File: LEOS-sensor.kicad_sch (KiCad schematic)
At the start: 3 parts

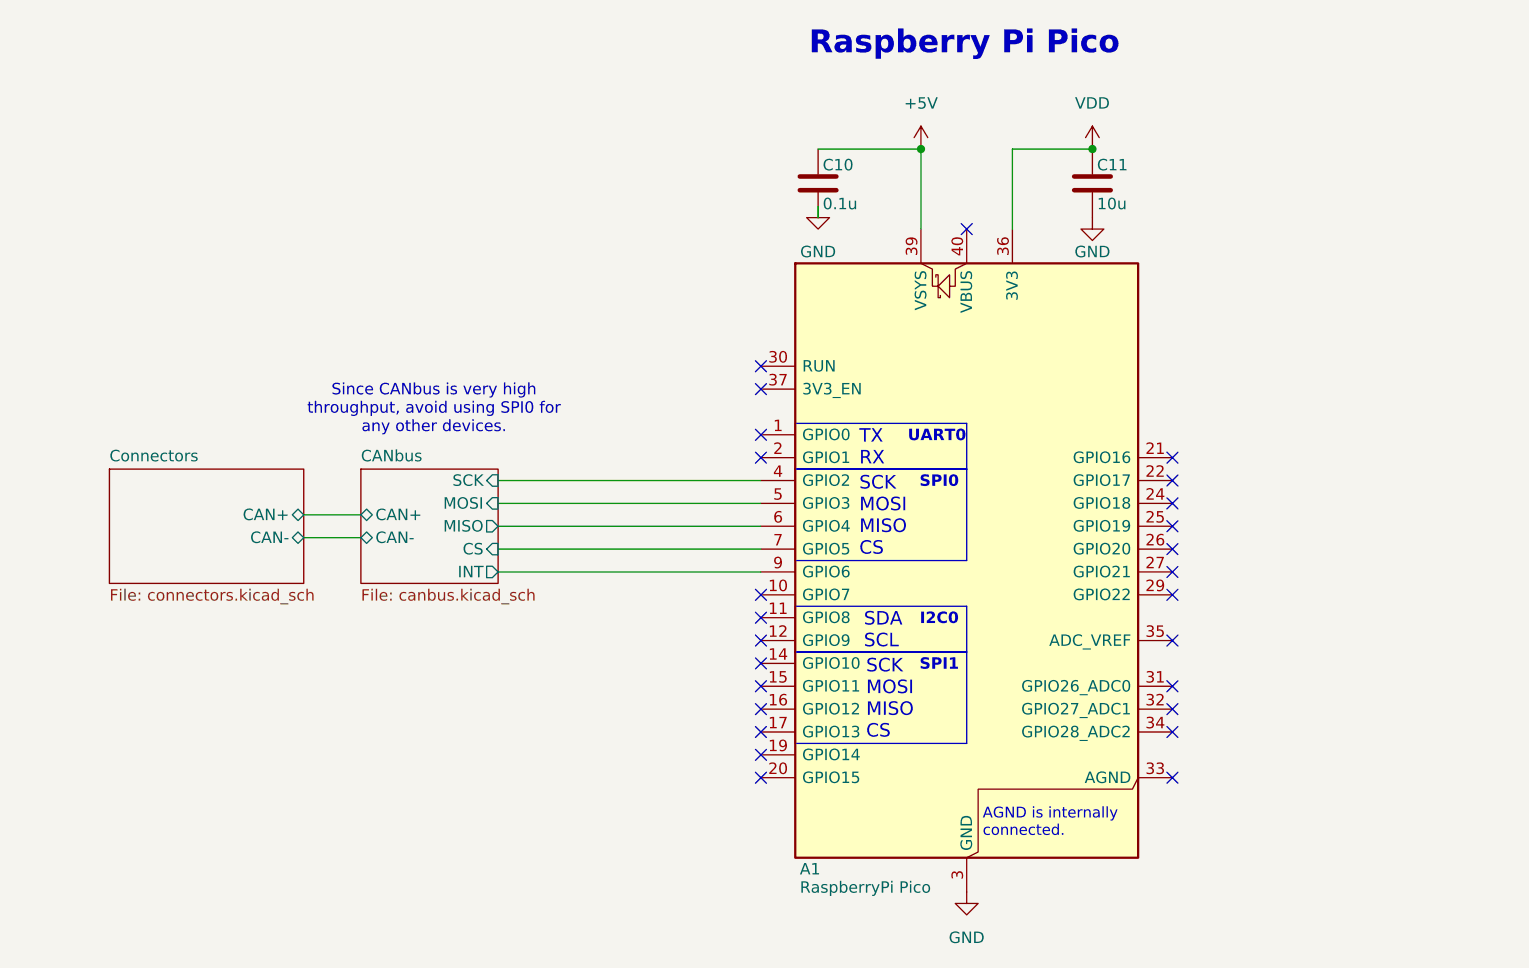
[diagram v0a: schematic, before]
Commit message: Updated from template, added graphics and JST-XH connectors
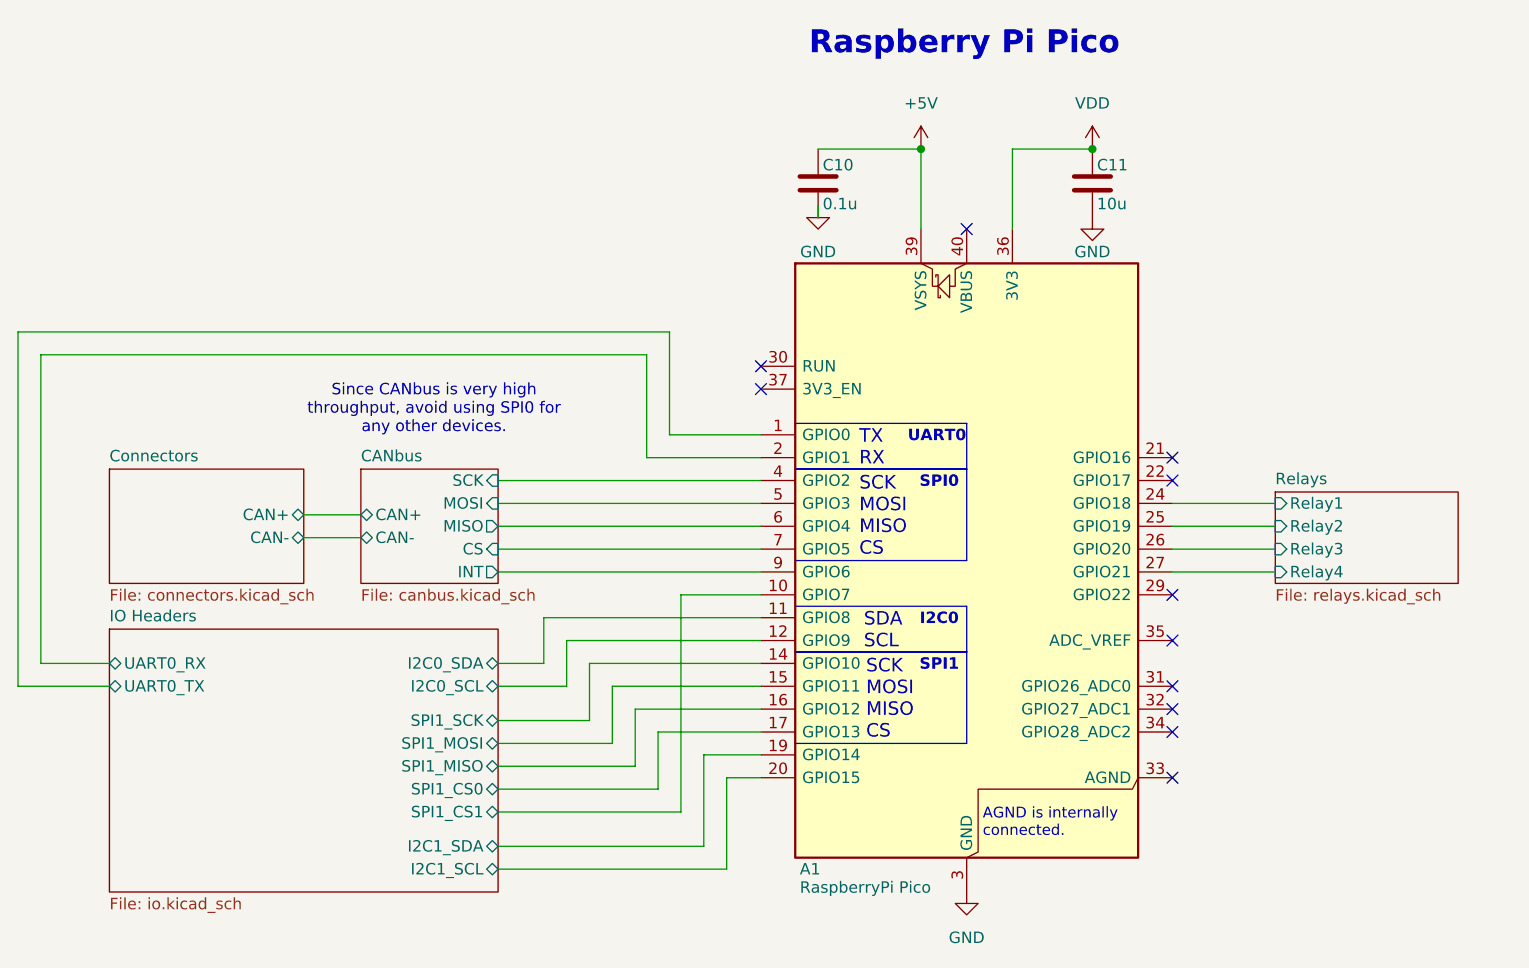
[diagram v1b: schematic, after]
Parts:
- C10: LCSC (none) -> C913912
- C11: LCSC (none) -> C95841
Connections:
- net IO Headers/UART0_TX: now reaches A1.1 (GPIO0)
- net IO Headers/SPI1_CS1: now reaches A1.10 (GPIO7)
- net IO Headers/I2C0_SDA: now reaches A1.11 (GPIO8)
- net IO Headers/I2C0_SCL: now reaches A1.12 (GPIO9)
- net IO Headers/SPI1_SCK: now reaches A1.14 (GPIO10)
- net IO Headers/SPI1_MOSI: now reaches A1.15 (GPIO11)
- net IO Headers/SPI1_MISO: now reaches A1.16 (GPIO12)
- net IO Headers/SPI1_CS0: now reaches A1.17 (GPIO13)
- net IO Headers/I2C1_SDA: now reaches A1.19 (GPIO14)
- net IO Headers/UART0_RX: now reaches A1.2 (GPIO1)
- net IO Headers/I2C1_SCL: now reaches A1.20 (GPIO15)
- net Relays/Relay1: now reaches A1.24 (GPIO18)
- net Relays/Relay2: now reaches A1.25 (GPIO19)
- net Relays/Relay3: now reaches A1.26 (GPIO20)
- net Relays/Relay4: now reaches A1.27 (GPIO21)
- no-connect marks 26 -> 11
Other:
- added sheet IO Headers (io.kicad_sch)
- added sheet Relays (relays.kicad_sch)
- title: LEOS Microcontroller -> LEOS Sensor Module

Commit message: Add production date and up revision
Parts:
- C10: Digikey 490-5798-1-ND -> 1276-CL10B104KB8NNNLCT-ND
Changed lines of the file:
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@@
 	(title_block
 		(title "LEOS Sensor Module")
-		(date "2026-02-15")
-		(rev "2")
+		(date "2026-02-17")
+		(rev "2.1")
 		(company "VIP Lightning From the Edge of Space")
 	)
@@
 			)
 		)
-		(property "Digikey" "490-5798-1-ND"
+		(property "Digikey" "1276-CL10B104KB8NNNLCT-ND"
 			(at 130.81 60.96 0)
 			(effects
